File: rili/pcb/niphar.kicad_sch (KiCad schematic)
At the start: 0 parts

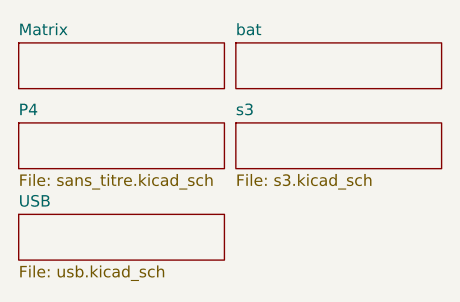
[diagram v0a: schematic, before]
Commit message: schéma v2 : coffre P4 complet — ERC 0 erreur
- Feuille p4 (ex sans_titre) : AMS1117-3.3 (rail P4_3V3 séparé, 10µF/22µF),
  CHIP_PU RC 100k+100nF, USB HS (ESP_USB_P/N) vers le port 2 du hub,
  microSD slot UHS-I (CLK/CMD/DAT0-3 sur GPIO39-44, pull-ups 10k),
  prog P4 via port 3 du hub (USB-Serial-JTAG + jumpers d'isolation)
- Périphériques : écran Sharp LS011B7DH03 (SPI partagé, CS_DPL=GPIO14),
  trackpad TPS43 (I2C 47/48, RDY=42, bloc généré+validé), C6 laissé vierge
  (OTA via P4 = voie officielle)
- Ménage ERC : 65 no_connect + 6 PWR_FLAG posés par script (fix_nc.py),
  labels fantômes S3P4 supprimés — ERC projet : 71 → 0 erreur,
  warnings 262 → 158 (ratchet enregistré)
- Hooks Claude Code Stop/PostToolUse désactivés (garde-fou = pre-push + CI)

Reste au schéma : le 2e MCU (moitié droite, col*_d/row*_d en attente).
DRC layout hors périmètre (chantier séparé).

Co-Authored-By: Claude Fable 5 <noreply@anthropic.com>
Claude-Session: https://claude.ai/code/session_01GfX5RmekmQi78Dm37qsT4Z
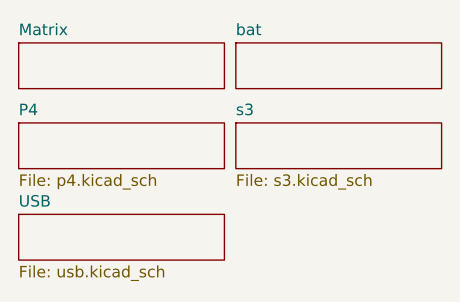
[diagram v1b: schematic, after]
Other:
- sheet P4: file sans_titre.kicad_sch -> p4.kicad_sch
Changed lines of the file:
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@@
 			)
 		)
-		(property "Sheetfile" "sans_titre.kicad_sch"
+		(property "Sheetfile" "p4.kicad_sch"
 			(at 17.78 33.6046 0)
 			(show_name no)
@@
 		)
 		(instances
-			(project "rili"
+			(project "niphar"
 				(path "/7138aad8-3c5f-41d0-9987-adc2f08f0576"
 					(page "4")
@@
 		)
 		(instances
-			(project "rili"
+			(project "niphar"
 				(path "/7138aad8-3c5f-41d0-9987-adc2f08f0576"
 					(page "6")
@@
 		)
 		(instances
-			(project "rili"
+			(project "niphar"
 				(path "/7138aad8-3c5f-41d0-9987-adc2f08f0576"
 					(page "2")
@@
 		)
 		(instances
-			(project "rili"
+			(project "niphar"
 				(path "/7138aad8-3c5f-41d0-9987-adc2f08f0576"
 					(page "3")
@@
 		)
 		(instances
-			(project "rili"
+			(project "niphar"
 				(path "/7138aad8-3c5f-41d0-9987-adc2f08f0576"
 					(page "5")

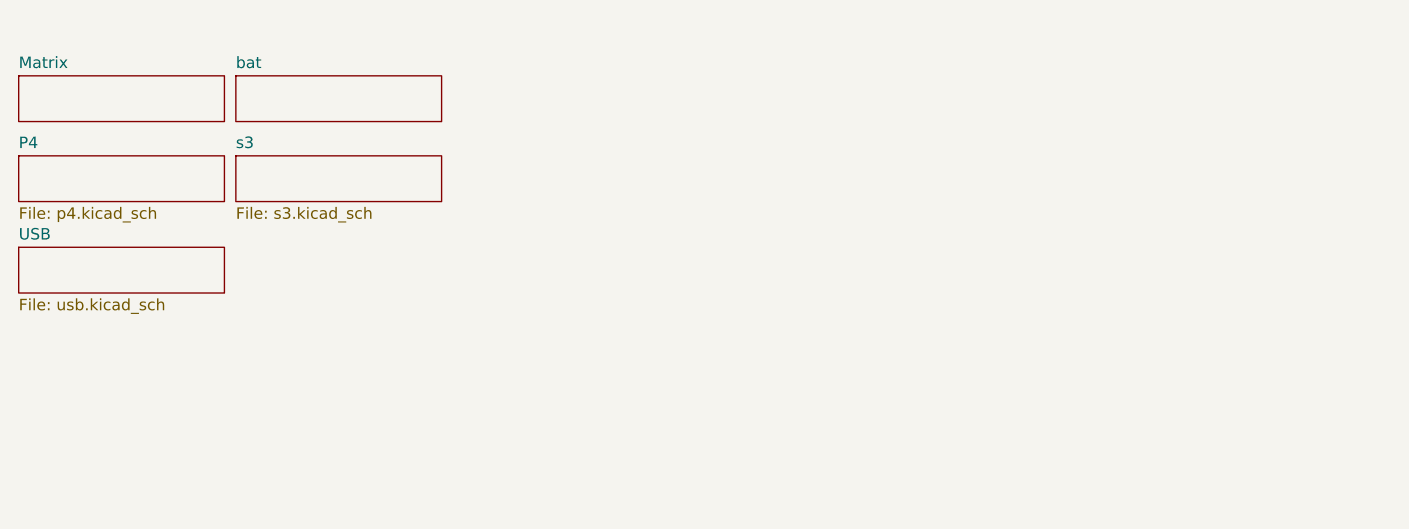
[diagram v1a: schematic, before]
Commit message: schéma v2 COMPLET : les deux moitiés — ERC 0 erreur
Architecture finale (brainstorm + nuit de réflexion, décision Mae) :
asymétrie d'origine confirmée — UN seul coffre.
- Gauche (s3/bat/usb/p4) : S3 + matrice + trackpad TPS43 + alim 16340
  + USB-C + hub CH334R + coffre P4 (SD multi-ISO, PGP, prog-via-hub)
- Droite (right/bat_right/usb_right, NOUVELLES feuilles) : S3 + matrice
  + écran Sharp + alim 16340 propre + USB-C simple (USBLC6 direct, sans hub)

Génération scriptée (make_droite/make_right_rails/cleanup, scratchpad) :
copies s3→right (refs +200) et bat→bat_right (refs +300, rails +BATT_D/
VSYS_D/+3.3V_D), usb→usb_right (refs +400, hub/P4/prog retirés, USBLC6
→ D±_s3_d, +5V_D), rails gauche/droite séparés (GND seul commun, physique
via TRRS), populate tranché (écran→droite, trackpad→gauche), feuille
Matrix retirée (matrice droite incluse dans right), droite.kicad_sch
remplacé par right.kicad_sch.

Validation : ERC projet 0 erreur ; nets droite bouclés de bout en bout
(+BATT_D→+3.3V_D→MCU, USB→USBLC6→MCU, jauge→GPIO13). Baseline warnings
re-référencée 125→164 (libs legacy doublées par la 2e moitié).

Prochaine phase : LAYOUT (réconciliation PCB↔schéma en une passe,
placement, routage, panneau sécable, DRC).

Co-Authored-By: Claude Fable 5 <noreply@anthropic.com>
Claude-Session: https://claude.ai/code/session_01GfX5RmekmQi78Dm37qsT4Z
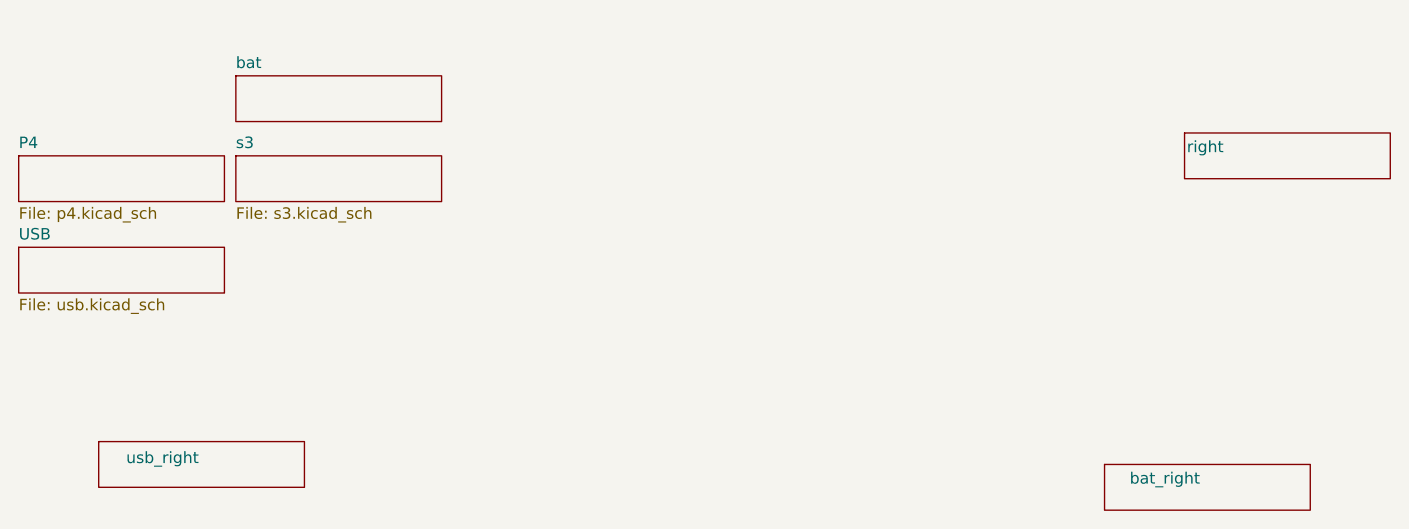
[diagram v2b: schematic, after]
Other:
- removed sheet Matrix
- added sheet bat_right (bat_right.kicad_sch)
- added sheet right (right.kicad_sch)
- added sheet usb_right (usb_right.kicad_sch)
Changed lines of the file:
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@@
 	)
 	(sheet
-		(at 17.78 19.05)
+		(at 147.32 25.4)
 		(size 22.86 5.08)
 		(exclude_from_sim no)
@@
 			(color 0 0 0 0)
 		)
-		(property "Sheetname" "Matrix"
-			(at 17.78 18.3384 0)
+		(property "Sheetname" "right"
+			(at 147.574 27.686 0)
 			(show_name no)
 			(do_not_autoplace no)
@@
 			)
 		)
-		(property "Sheetfile" "matrix.kicad_sch"
-			(at 17.018 24.638 0)
+		(property "Sheetfile" "right.kicad_sch"
+			(at 96.52 31.0646 0)
 			(hide yes)
 			(show_name no)
@@
 			(project "niphar"
 				(path "/7138aad8-3c5f-41d0-9987-adc2f08f0576"
-					(page "6")
+					(page "2")
+				)
+			)
+		)
+	)
+	(sheet
+		(at 138.43 62.23)
+		(size 22.86 5.08)
+		(exclude_from_sim no)
+		(in_bom yes)
+		(on_board yes)
+		(dnp no)
+		(stroke
+			(width 0.1524)
+			(type solid)
+		)
+		(fill
+			(color 0 0 0 0)
+		)
+		(property "Sheetname" "bat_right"
+			(at 141.224 64.516 0)
+			(show_name no)
+			(do_not_autoplace no)
+			(effects
+				(font
+					(size 1.27 1.27)
+				)
+				(justify left bottom)
+			)
+		)
+		(property "Sheetfile" "bat_right.kicad_sch"
+			(at 87.63 42.4946 0)
+			(hide yes)
+			(show_name no)
+			(do_not_autoplace no)
+			(effects
+				(font
+					(size 1.27 1.27)
+				)
+				(justify left top)
+			)
+		)
+		(instances
+			(project "niphar"
+				(path "/7138aad8-3c5f-41d0-9987-adc2f08f0576"
+					(page "5")
 				)
 			)
@@
 				)
 			)
+		)
+	)
+	(sheet
+		(at 26.67 59.69)
+		(size 22.86 5.08)
+		(exclude_from_sim no)
+		(in_bom yes)
+		(on_board yes)
+		(dnp no)
+		(stroke
+			(width 0.1524)
+			(type solid)
+		)
+		(fill
+			(color 0 0 0 0)
+		)
+		(property "Sheetname" "usb_right"
+			(at 29.718 62.23 0)
+			(show_name no)
+			(do_not_autoplace no)
+			(effects
+				(font
+					(size 1.27 1.27)
+				)
+				(justify left bottom)
+			)
+		)
+		(property "Sheetfile" "usb_right.kicad_sch"
+			(at -24.13 39.9546 0)
+			(hide yes)
+			(show_name no)
+			(do_not_autoplace no)
+			(effects
+				(font
+					(size 1.27 1.27)
+				)
+				(justify left top)
+			)
+		)
+		(instances
+			(project "niphar"
+				(path "/7138aad8-3c5f-41d0-9987-adc2f08f0576"
+					(page "3")
+				)
+			)

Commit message: layout v2 : carte routée — PCB↔schéma réconciliés, BOM LCSC, TVS matrice, DRC 990→24
- réconciliation PCB↔schéma en une passe : 105 empreintes remariées (matrice ×2,
  module P4), 54 périmées supprimées, ~140 importées par F8 ; footprint TRRS
  MJ-4PP-9_rev3 créé (pads mappés de l'ancien design fonctionnel)
- placement : moitié droite générée au miroir exact du pré-placement gauche
  (axe x=188.46048), trous de montage symétrisés, origine de grille sur l'axe
- protection ESD matrice : 22 SD05C-01F (un par ligne, côté switchs des 100R,
  validés par partition de netlist) ; PWR_FLAG +5V_D réparé
- BOM LCSC dans les propriétés des symboles (32 composants : réfs, liens,
  notes d'achat) + annexe courses complète au plan v2 ; connecteur trackpad
  corrigé (ZIF Hirose FH12-6S-0.5SH, réf MNT Reform)
- règles JLCPCB (planchers DRC + classes Default/Power re-branchées v2),
  passage 4 couches, routage complet des deux moitiés
- gerbers v1 corne-cherry retirés (obsolètes)
- baselines tripwire re-référencées : DRC 990→24 erreurs / 208→17 warnings,
  ERC 0 erreur / 200 warnings (53 fantômes headless documentés)

Co-Authored-By: Claude Fable 5 <noreply@anthropic.com>
Claude-Session: https://claude.ai/code/session_01GfX5RmekmQi78Dm37qsT4Z
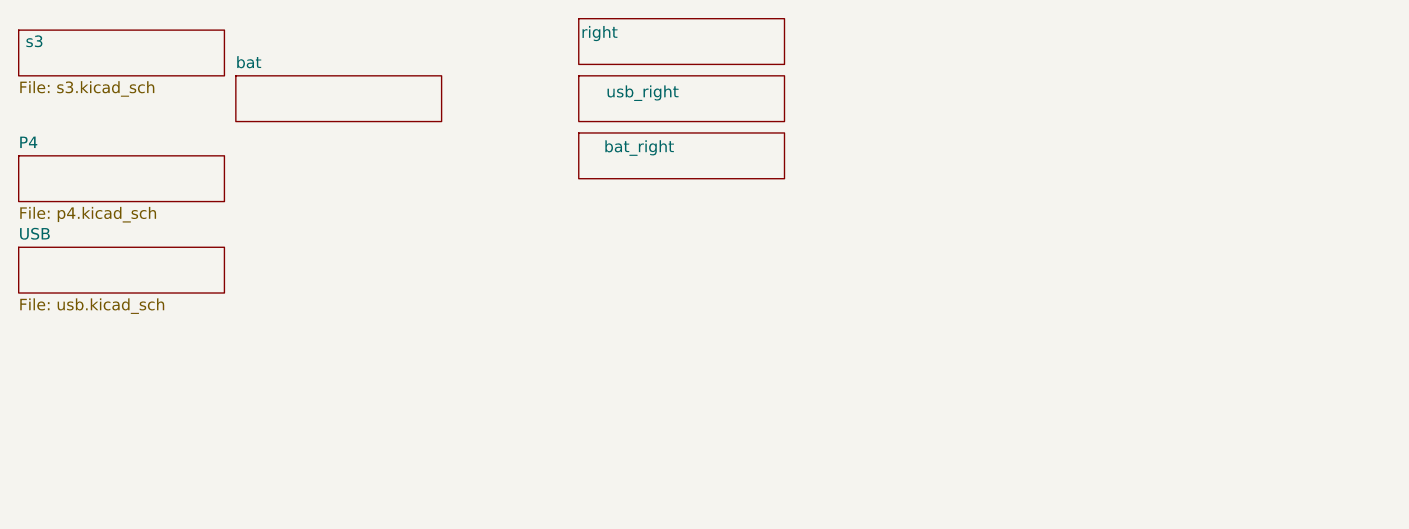
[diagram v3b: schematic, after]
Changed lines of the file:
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@@
 	)
 	(sheet
-		(at 147.32 25.4)
+		(at 80.01 12.7)
 		(size 22.86 5.08)
 		(exclude_from_sim no)
@@
 		)
 		(property "Sheetname" "right"
-			(at 147.574 27.686 0)
+			(at 80.264 14.986 0)
 			(show_name no)
 			(do_not_autoplace no)
@@
 		)
 		(property "Sheetfile" "right.kicad_sch"
-			(at 96.52 31.0646 0)
+			(at 29.21 18.3646 0)
 			(hide yes)
+			(show_name no)
+			(do_not_autoplace no)
+			(effects
+				(font
+					(size 1.27 1.27)
+				)
+				(justify left top)
+			)
+		)
+		(instances
+			(project "niphar"
+				(path "/7138aad8-3c5f-41d0-9987-adc2f08f0576"
+					(page "6")
+				)
+			)
+		)
+	)
+	(sheet
+		(at 80.01 25.4)
+		(size 22.86 5.08)
+		(exclude_from_sim no)
+		(in_bom yes)
+		(on_board yes)
+		(dnp no)
+		(stroke
+			(width 0.1524)
+			(type solid)
+		)
+		(fill
+			(color 0 0 0 0)
+		)
+		(property "Sheetname" "bat_right"
+			(at 82.804 27.686 0)
+			(show_name no)
+			(do_not_autoplace no)
+			(effects
+				(font
+					(size 1.27 1.27)
+				)
+				(justify left bottom)
+			)
+		)
+		(property "Sheetfile" "bat_right.kicad_sch"
+			(at 29.21 5.6646 0)
+			(hide yes)
+			(show_name no)
+			(do_not_autoplace no)
+			(effects
+				(font
+					(size 1.27 1.27)
+				)
+				(justify left top)
+			)
+		)
+		(instances
+			(project "niphar"
+				(path "/7138aad8-3c5f-41d0-9987-adc2f08f0576"
+					(page "8")
+				)
+			)
+		)
+	)
+	(sheet
+		(at 17.78 13.97)
+		(size 22.86 5.08)
+		(exclude_from_sim no)
+		(in_bom yes)
+		(on_board yes)
+		(dnp no)
+		(stroke
+			(width 0.1524)
+			(type solid)
+		)
+		(fill
+			(color 0 0 0 0)
+		)
+		(property "Sheetname" "s3"
+			(at 18.542 16.002 0)
+			(show_name no)
+			(do_not_autoplace no)
+			(effects
+				(font
+					(size 1.27 1.27)
+				)
+				(justify left bottom)
+			)
+		)
+		(property "Sheetfile" "s3.kicad_sch"
+			(at 17.78 19.6346 0)
 			(show_name no)
 			(do_not_autoplace no)
@@
 	)
 	(sheet
-		(at 138.43 62.23)
+		(at 80.01 19.05)
 		(size 22.86 5.08)
 		(exclude_from_sim no)
@@
 			(color 0 0 0 0)
 		)
-		(property "Sheetname" "bat_right"
-			(at 141.224 64.516 0)
+		(property "Sheetname" "usb_right"
+			(at 83.058 21.59 0)
 			(show_name no)
 			(do_not_autoplace no)
@@
 			)
 		)
-		(property "Sheetfile" "bat_right.kicad_sch"
-			(at 87.63 42.4946 0)
+		(property "Sheetfile" "usb_right.kicad_sch"
+			(at 29.21 -0.6854 0)
 			(hide yes)
 			(show_name no)
@@
 			(project "niphar"
 				(path "/7138aad8-3c5f-41d0-9987-adc2f08f0576"
-					(page "5")
+					(page "7")
 				)
 			)
-		)
-	)
-	(sheet
-		(at 41.91 27.94)
-		(size 22.86 5.08)
-		(exclude_from_sim no)
-		(in_bom yes)
-		(on_board yes)
-		(dnp no)
-		(fields_autoplaced yes)
-		(stroke
-			(width 0.1524)
-			(type solid)
-		)
-		(fill
-			(color 0 0 0 0)
-		)
-		(property "Sheetname" "s3"
-			(at 41.91 27.2284 0)
-			(show_name no)
-			(do_not_autoplace no)
-			(effects
-				(font
-					(size 1.27 1.27)
-				)
-				(justify left bottom)
-			)
-		)
-		(property "Sheetfile" "s3.kicad_sch"
-			(at 41.91 33.6046 0)
-			(show_name no)
-			(do_not_autoplace no)
-			(effects
-				(font
-					(size 1.27 1.27)
-				)
-				(justify left top)
-			)
-		)
-		(instances
-			(project "niphar"
-				(path "/7138aad8-3c5f-41d0-9987-adc2f08f0576"
-					(page "2")
-				)
-			)
-		)
-	)
-	(sheet
-		(at 26.67 59.69)
-		(size 22.86 5.08)
-		(exclude_from_sim no)
-		(in_bom yes)
-		(on_board yes)
-		(dnp no)
-		(stroke
-			(width 0.1524)
-			(type solid)
-		)
-		(fill
-			(color 0 0 0 0)
-		)
-		(property "Sheetname" "usb_right"
-			(at 29.718 62.23 0)
-			(show_name no)
-			(do_not_autoplace no)
-			(effects
-				(font
-					(size 1.27 1.27)
-				)
-				(justify left bottom)
-			)
-		)
-		(property "Sheetfile" "usb_right.kicad_sch"
-			(at -24.13 39.9546 0)
-			(hide yes)
-			(show_name no)
-			(do_not_autoplace no)
-			(effects
-				(font
-					(size 1.27 1.27)
-				)
-				(justify left top)
-			)
-		)
-		(instances
-			(project "niphar"
-				(path "/7138aad8-3c5f-41d0-9987-adc2f08f0576"
-					(page "3")
-				)
-			)
